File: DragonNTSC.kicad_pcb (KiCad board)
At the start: 2 copper layers, 120.2 x 35.7 mm, 19 parts, among them IC1 74LS273N, IC2 MC6847, IC3 MC1372, J1 Video Output, J2 Board Interconnect Male, Q1 2N4403, Q2 2N4401

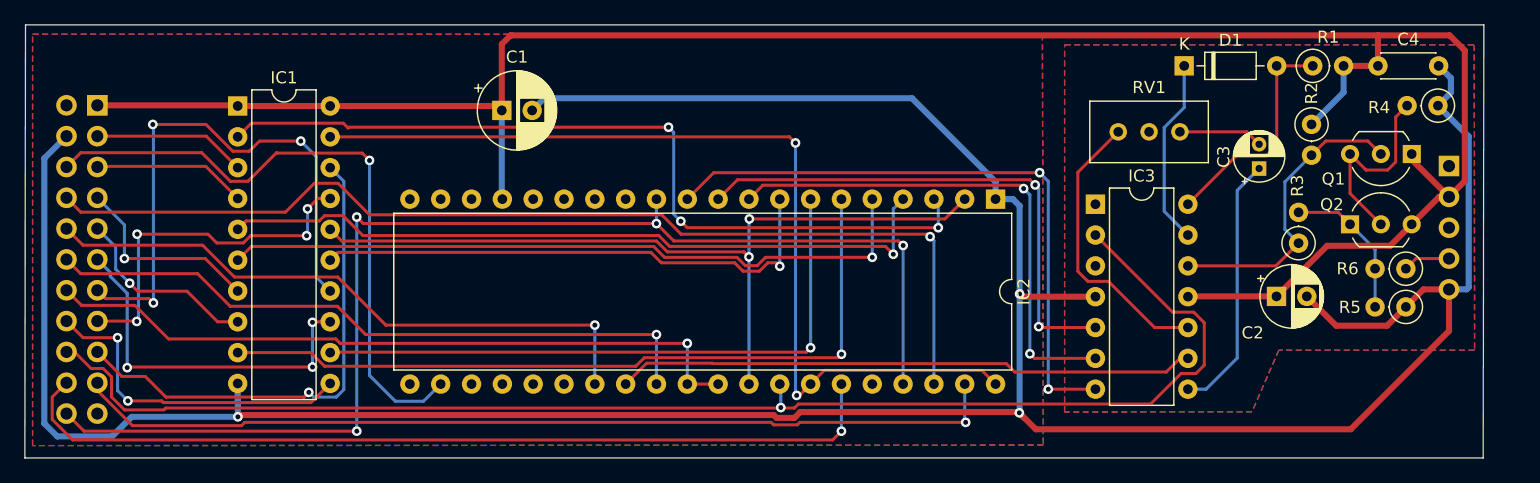
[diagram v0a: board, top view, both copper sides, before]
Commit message: add 555 timer
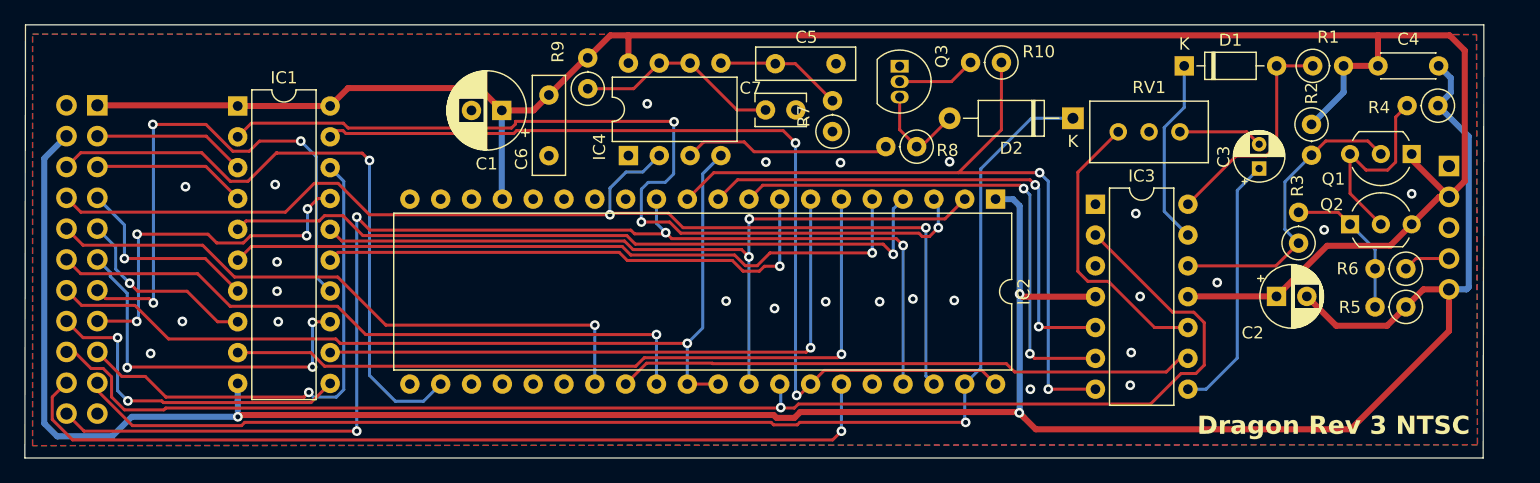
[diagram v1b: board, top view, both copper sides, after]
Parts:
- added C5: .022uF, Capacitor_THT:C_Disc_D8.0mm_W2.5mm_P5.00mm, F.Cu at (143.2, 100.2)
- added C6: .022uF, Capacitor_THT:C_Disc_D8.0mm_W2.5mm_P5.00mm, F.Cu at (124.5, 107.8)
- added C7: .001uF, Capacitor_THT:C_Rect_L4.0mm_W2.5mm_P2.50mm, F.Cu at (142.4, 104.0)
- added D2: 1KF20-04, Diode_THT:D_A-405_P10.16mm_Horizontal, F.Cu at (167.7, 104.7)
- added IC4: NE555P, Package_DIP:DIP-8_W7.62mm, F.Cu at (131.1, 107.8)
- added Q3: 2N3904, Package_TO_SOT_THT:TO-92_Inline, F.Cu at (153.4, 100.4)
- added R10: 1K, Resistor_THT:R_Axial_DIN0207_L6.3mm_D2.5mm_P2.54mm_Vertical, F.Cu at (161.8, 100.1)
- added R7: 2.2K, Resistor_THT:R_Axial_DIN0207_L6.3mm_D2.5mm_P2.54mm_Vertical, F.Cu at (147.9, 105.8)
- added R8: 4.7K, Resistor_THT:R_Axial_DIN0207_L6.3mm_D2.5mm_P2.54mm_Vertical, F.Cu at (154.8, 107.0)
- added R9: 9.1k, Resistor_THT:R_Axial_DIN0207_L6.3mm_D2.5mm_P2.54mm_Vertical, F.Cu at (127.7, 102.3)
- turned C1 to 180 degrees
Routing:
- net GND: track 257.2 -> 214.4 mm, vias 3 -> 28
- net CSS: track 76.9 -> 104.5 mm
- net Net-(IC4-DIS): track 0.00 -> 17.1 mm
- net Net-(IC4-Q): track 0.00 -> 17.1 mm
- net GM0: track 58.9 -> 75.5 mm
- net phiA: track 52.0 -> 62.5 mm
- net Net-(IC4-CV): track 0.00 -> 10.5 mm
- net Net-(D2-A): track 0.00 -> 8.36 mm
- net ~{HS}: track 86.7 -> 94.4 mm, vias 1 -> 2
- net Net-(IC1-Q0): track 68.3 -> 74.9 mm
- net Net-(Q3-C): track 0.00 -> 6.50 mm
- net ~{FS}: track 101.6 -> 102.8 mm
- net Net-(IC1-Q7): track 77.1 -> 77.7 mm
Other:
- board text added: "Dragon Rev 3 NTSC"

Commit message: migrate to kicad 9
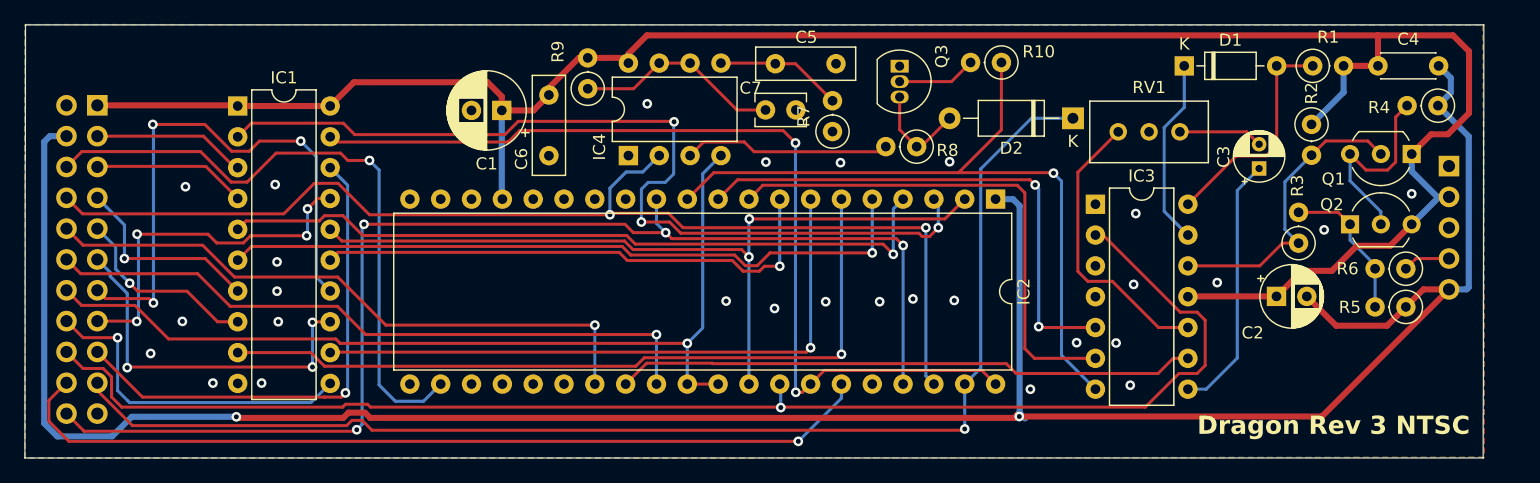
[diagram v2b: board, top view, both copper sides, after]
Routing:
- net GND: track 214.4 -> 203.5 mm, vias 28 -> 30
- net phiA: track 62.5 -> 60.9 mm, vias 2 -> 1
- net ~{FS}: track 102.8 -> 101.5 mm
- net ~{A}/G: track 73.5 -> 72.5 mm
- net CSS: track 104.5 -> 105.2 mm
- net +5V: track 180.4 -> 179.9 mm
- net CHB: track 42.6 -> 42.5 mm, vias 2 -> 0
- net ~{RAS0}: vias 2 -> 1

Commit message: revise for fab
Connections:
- J1 pad 3: unconnected-(J1-Pin_3-Pad3) -> -5V
- J2 pad 2: -5V -> unconnected-(J2-Pin_2-Pad2)
- RV1 pad 1: Net-(C3-Pad2) -> unconnected-(RV1-Pad1)
- RV1 pad 2: unconnected-(RV1-Pad2) -> Net-(C3-Pad2)
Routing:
- net GND: track 203.5 -> 0.00 mm, vias 30 -> 0
- net +5V: track 179.9 -> 0.06 mm
- net DO5: track 46.6 -> 20.1 mm, vias 3 -> 1
- net DO4: track 30.4 -> 24.4 mm, vias 3 -> 0
- net Net-(C3-Pad2): track 6.95 -> 10.9 mm
- net Net-(D1-K): track 15.4 -> 17.6 mm
- net DO6: track 29.5 -> 27.5 mm, vias 4 -> 1
- net Net-(IC1-Q0): track 75.2 -> 73.2 mm, vias 3 -> 2
- net CSS: track 105.2 -> 103.4 mm
- net Net-(IC1-Q7): track 77.6 -> 75.9 mm, vias 2 -> 0
- net VCLK: track 116.0 -> 115.7 mm, vias 1 -> 0
- net phiB: track 43.5 -> 43.2 mm, vias 2 -> 0
- net ~{HS}: vias 2 -> 1
- net ~{RAS0}: vias 1 -> 0
- net ~{A}/G: vias 1 -> 0
- added copper zone on In2.Cu, net +5V
- added copper zone on In1.Cu, net GND
- removed copper zone on B.Cu, net GND
- removed copper zone on F.Cu, net GND
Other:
- copper layers 2 -> 4
